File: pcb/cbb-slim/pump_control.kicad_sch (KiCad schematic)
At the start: 6 parts, among them Q10 AO3400A

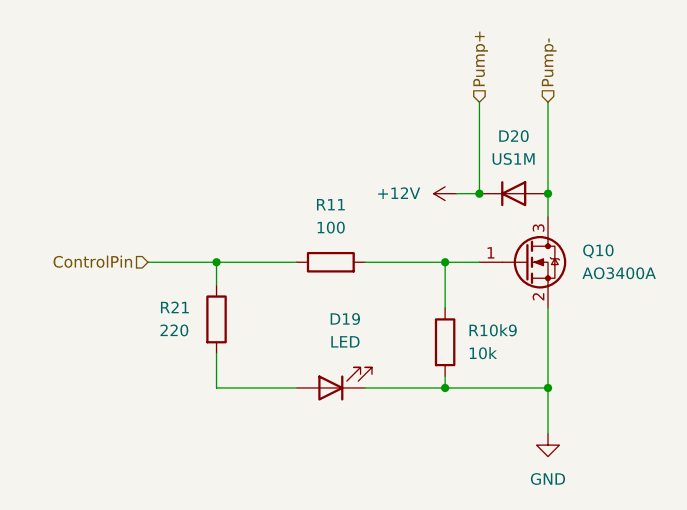
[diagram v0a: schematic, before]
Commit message: reduce brightness of channel indicator led
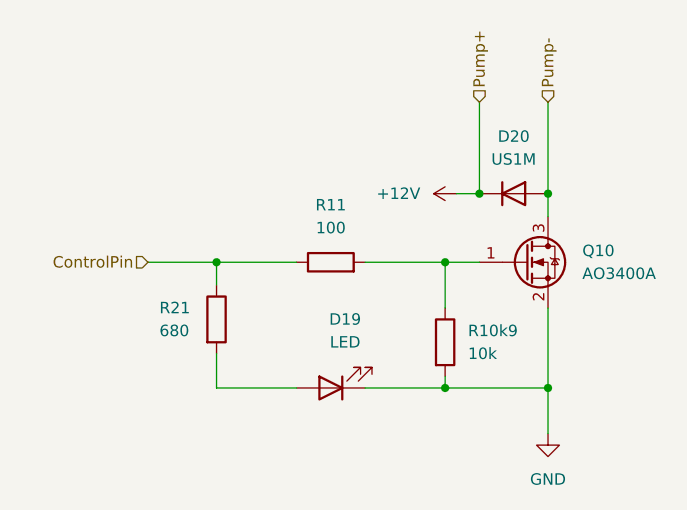
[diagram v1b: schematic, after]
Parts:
- R21: value 220 -> 680; mpn C22962 -> C23228
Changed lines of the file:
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@@
 			)
 		)
-		(property "Value" "220"
+		(property "Value" "680"
 			(at 92.71 90.17 0)
 			(effects
@@
 			)
 		)
-		(property "mpn" "C22962"
+		(property "mpn" "C23228"
 			(at 99.06 88.9 90)
 			(effects
@@
 		)
 		(instances
+			(project ""
+				(path "/08e8e2b9-5c8d-4651-bb52-679dee8728f5"
+					(reference "R21")
+					(unit 1)
+				)
+			)
 			(project ""
 				(path "/5575e3e9-07ff-42ca-b261-f5e11b540bc9/3efc0a38-659d-40fd-bced-46685d813a4e"
@@
 		)
 	)
+	(sheet_instances
+		(path "/"
+			(page "1")
+		)
+	)
